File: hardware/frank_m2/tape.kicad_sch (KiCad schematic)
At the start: 11 parts, among them Q1 BC850, Q2 BC850

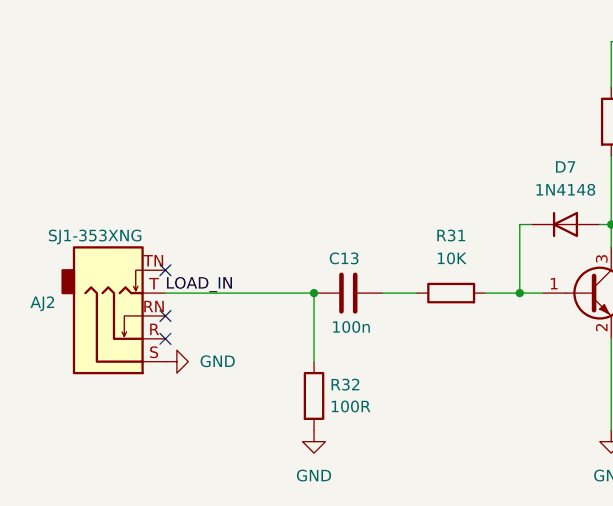
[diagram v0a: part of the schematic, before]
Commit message: Fixed tape loading bug on all PCBs
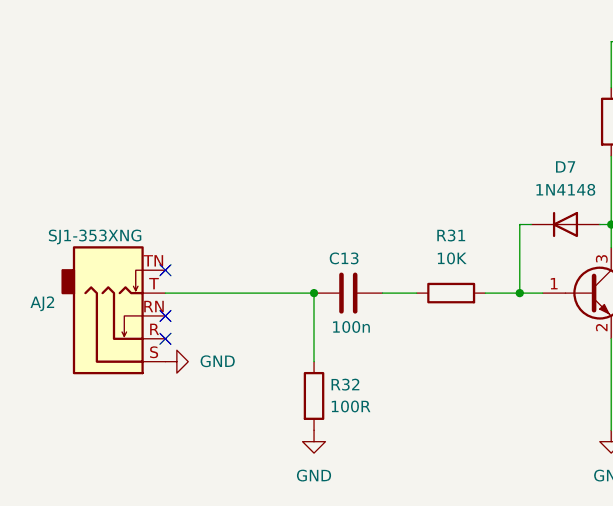
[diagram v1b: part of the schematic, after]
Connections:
- net LOAD_IN: no longer AJ2.T, C13.1, R32.1
- new net: AJ2.T, C13.1, R32.1
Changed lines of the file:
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@@
 	(title_block
 		(title "FRANK M2")
-		(date "2025-03-04")
-		(rev "1.02")
+		(date "2025-03-16")
+		(rev "1.03")
 		(company "Mikhail Matveev")
 		(comment 1 "https://github.com/xtremespb/frank")
@@
 		)
 	)
-	(label "LOAD_IN"
-		(at 49.53 72.39 0)
-		(effects
-			(font
-				(size 1.27 1.27)
-			)
-			(justify left bottom)
-		)
-	)

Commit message: Minor updates
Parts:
- renumbered C12 to C11, C13 to C12, AJ2 to J11
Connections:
- no-connect marks 3 -> 1
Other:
- note removed: "This schematics is used to load data from external audio source, e.g. tape."
- moved on the sheet: C11, C12, D7, Q1, Q2, R28, R29, R30, R31, R32
